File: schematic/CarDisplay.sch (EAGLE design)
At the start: 9 parts

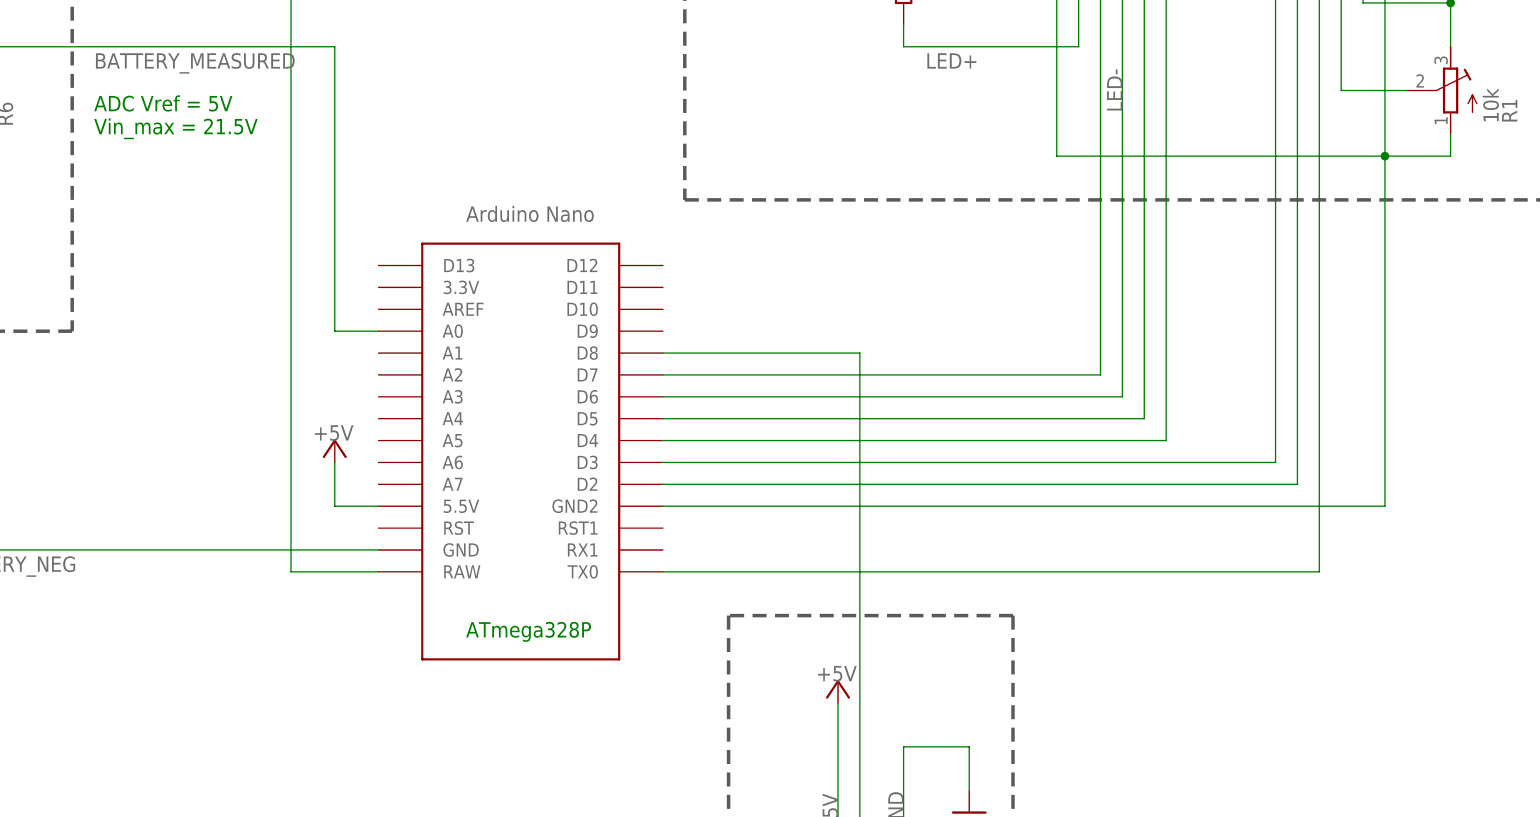
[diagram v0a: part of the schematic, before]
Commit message: Schematic update: the arudino nano component is replaced by better one
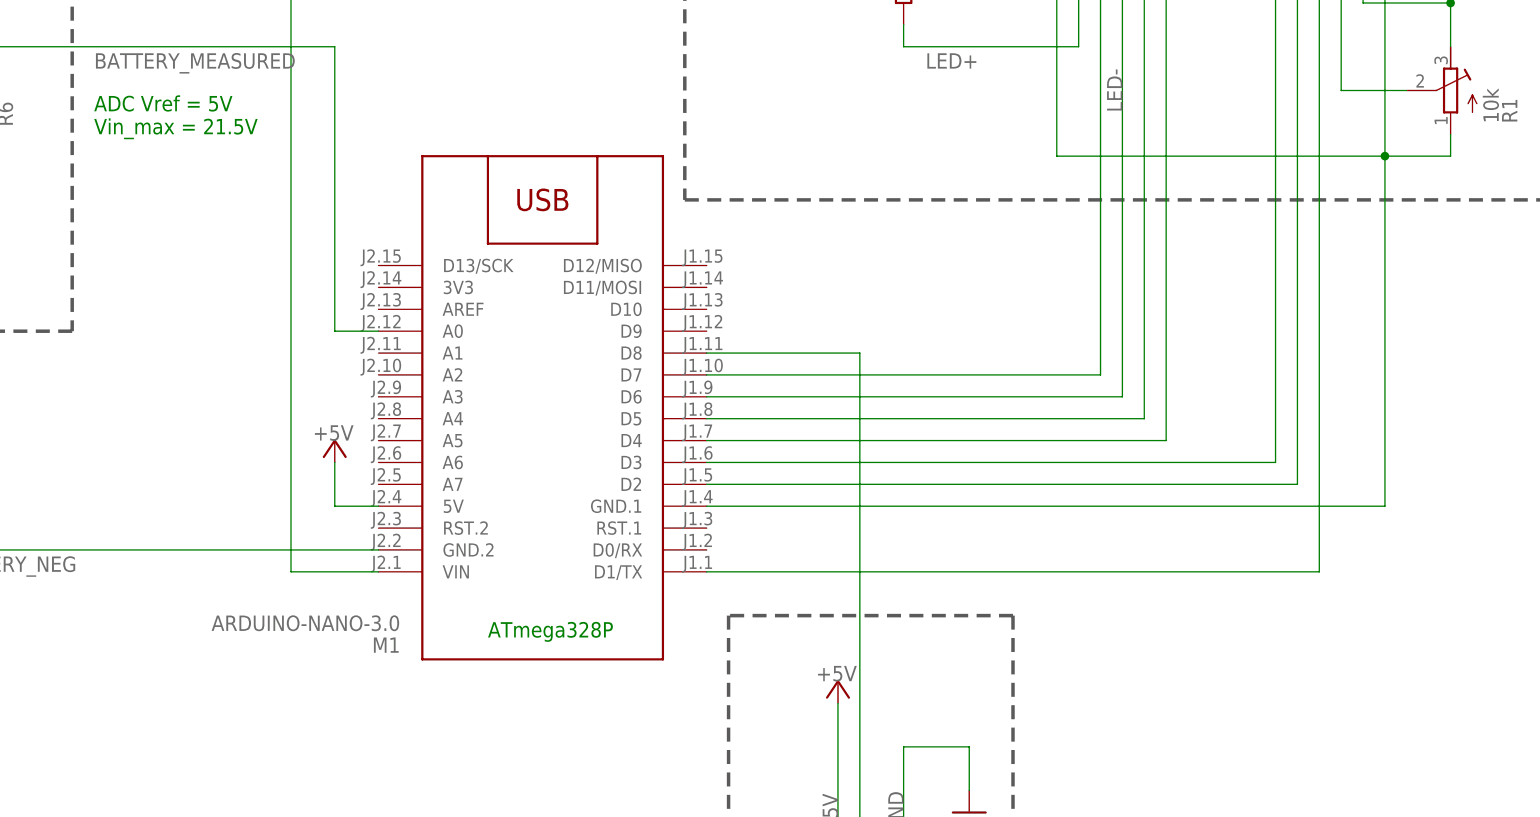
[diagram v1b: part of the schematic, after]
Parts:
- removed U$1: NANO, Arduino-clone:NANO
- added M1: ARDUINO-NANO-3.0, diy-modules:ARDUINO-NANO-3.0
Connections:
- net +5V: now also M1.5V; no longer U$1.5.5V
- net BATTERY_MEASURED: now also M1.A0; no longer U$1.A0
- net BATTERY_NEG: now also M1.GND.2; no longer U$1.GND
- net BATTERY_POS: now also M1.VIN; no longer U$1.RAW
- net LED-: now also M1.GND.1; no longer U$1.GND2
- net N$1: now also M1.D3
- net N$2: now also M1.D2
- net N$3: now also M1.D1/TX
- net N$4: now also M1.D7
- net N$5: now also M1.D6
- net N$6: now also M1.D5
- net N$7: now also M1.D4
- net N$8: now also M1.D8; no longer U$1.D8

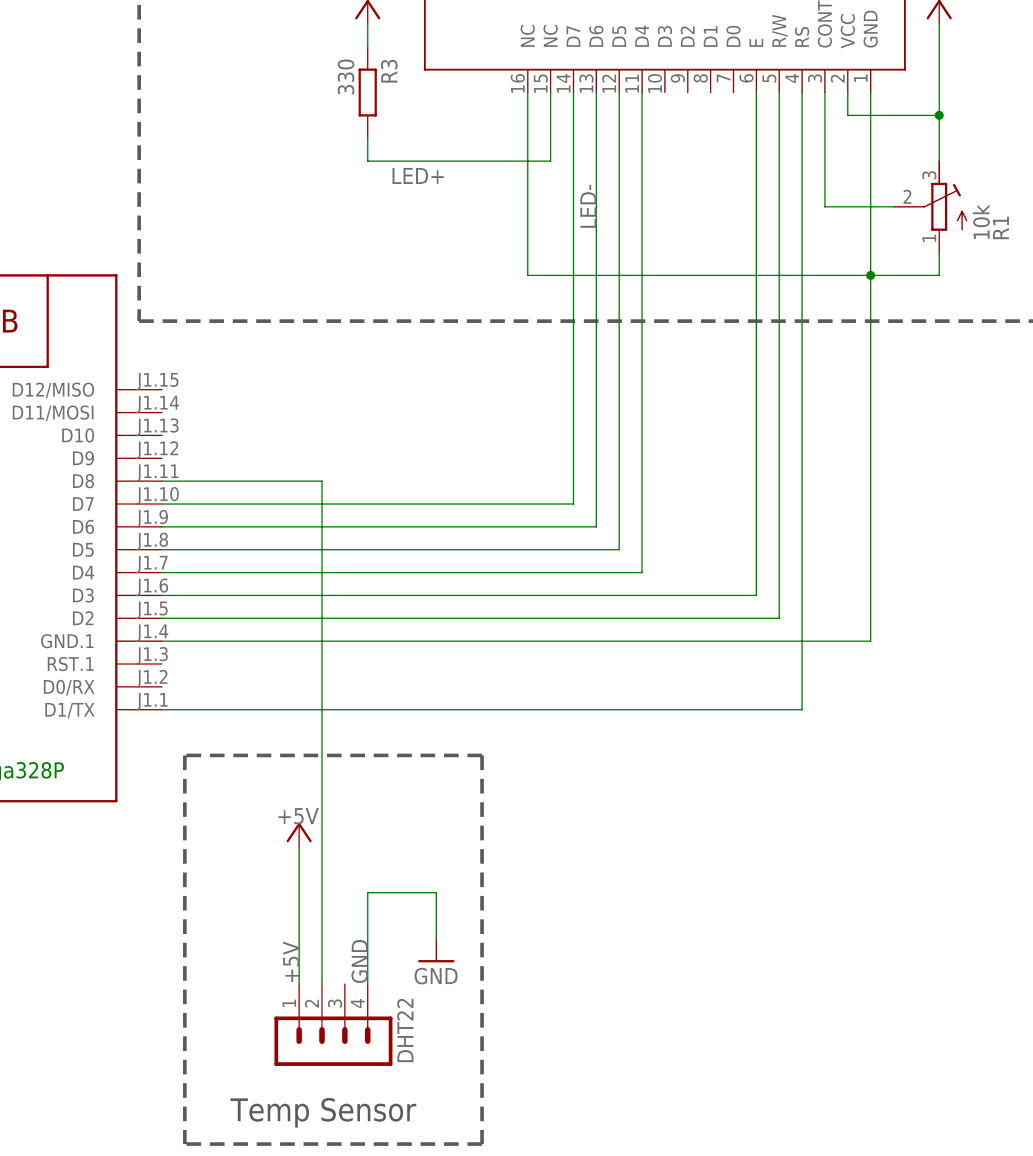
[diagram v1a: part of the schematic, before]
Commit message: Finalized elements: - schematic - utility documents - corrected code comments
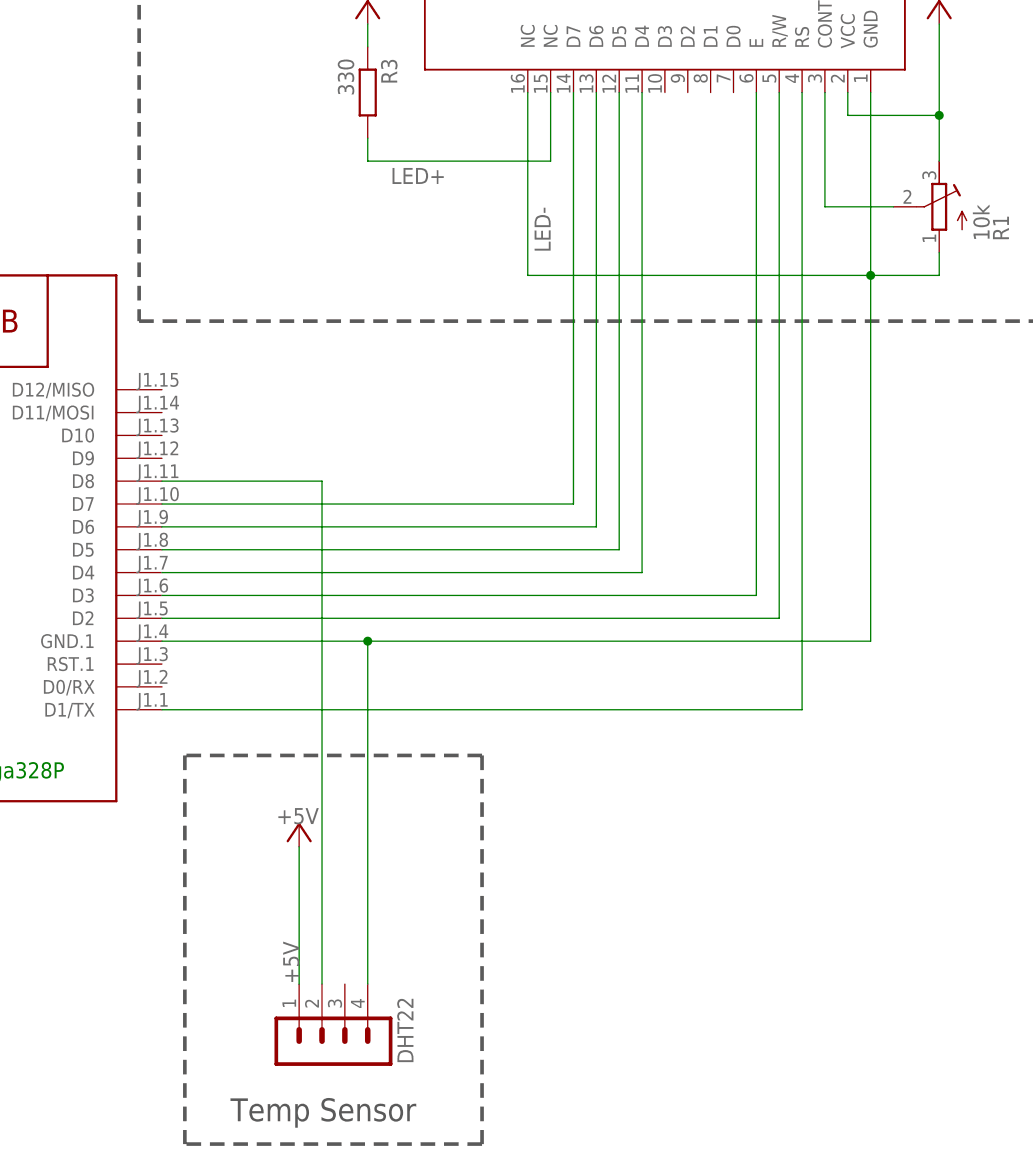
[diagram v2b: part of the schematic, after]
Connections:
- removed net GND: DHT22.4
- net LED-: now also DHT22.4
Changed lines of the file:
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@@
 <part name="R6" library="rcl" deviceset="R-EU_" device="0204/7" value="10k"/>
 <part name="DHT22" library="con-lstb" deviceset="MA04-1" device=""/>
-<part name="GND8" library="supply1" deviceset="GND" device=""/>
 <part name="C4" library="rcl" deviceset="CPOL-EU" device="E5-8.5" value="10u"/>
 <part name="R1" library="resistor" deviceset="R-TRIMM" device="3202" value="10k"/>
@@
 <instance part="R6" gate="G$1" x="66.04" y="127" rot="R270"/>
 <instance part="DHT22" gate="1" x="170.18" y="38.1" rot="MR90"/>
-<instance part="GND8" gate="1" x="180.34" y="48.26"/>
 <instance part="C4" gate="G$1" x="55.88" y="129.54" smashed="yes">
 <attribute name="VALUE" x="51.2826" y="130.937" size="1.778" layer="96" rot="R270"/>
@@
 <label x="165.1" y="45.72" size="1.778" layer="95" rot="R90"/>
 <pinref part="P+2" gate="1" pin="+5V"/>
-</segment>
-</net>
-<net name="GND" class="0">
-<segment>
-<pinref part="DHT22" gate="1" pin="4"/>
-<wire x1="172.72" y1="45.72" x2="172.72" y2="55.88" width="0.1524" layer="91"/>
-<wire x1="172.72" y1="55.88" x2="180.34" y2="55.88" width="0.1524" layer="91"/>
-<pinref part="GND8" gate="1" pin="GND"/>
-<wire x1="180.34" y1="55.88" x2="180.34" y2="50.8" width="0.1524" layer="91"/>
-<label x="172.72" y="45.72" size="1.778" layer="95" rot="R90"/>
 </segment>
 </net>
@@
 <wire x1="236.22" y1="124.46" x2="228.6" y2="124.46" width="0.1524" layer="91"/>
 <wire x1="228.6" y1="124.46" x2="228.6" y2="83.82" width="0.1524" layer="91"/>
-<wire x1="228.6" y1="83.82" x2="149.86" y2="83.82" width="0.1524" layer="91"/>
+<wire x1="228.6" y1="83.82" x2="172.72" y2="83.82" width="0.1524" layer="91"/>
+<wire x1="172.72" y1="83.82" x2="149.86" y2="83.82" width="0.1524" layer="91"/>
 <wire x1="190.5" y1="124.46" x2="228.6" y2="124.46" width="0.1524" layer="91"/>
-<label x="198.12" y="129.54" size="1.778" layer="95" rot="R90"/>
+<label x="193.04" y="127" size="1.778" layer="95" rot="R90"/>
 <pinref part="M1" gate="G$1" pin="GND.1"/>
-</segment>
-</net>
+<pinref part="DHT22" gate="1" pin="4"/>
+<wire x1="172.72" y1="45.72" x2="172.72" y2="83.82" width="0.1524" layer="91"/>
+<junction x="172.72" y="83.82"/>
+</segment>
+</net>
